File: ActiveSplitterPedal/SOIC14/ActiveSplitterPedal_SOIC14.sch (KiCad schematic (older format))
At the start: 9 parts, among them J1 MonoJack2Switch, J2 MonoJack2Switch, J3 MonoJack2Switch, J4 MonoJack2Switch, J5 MonoJack2Switch, J6 Barrel_Jack

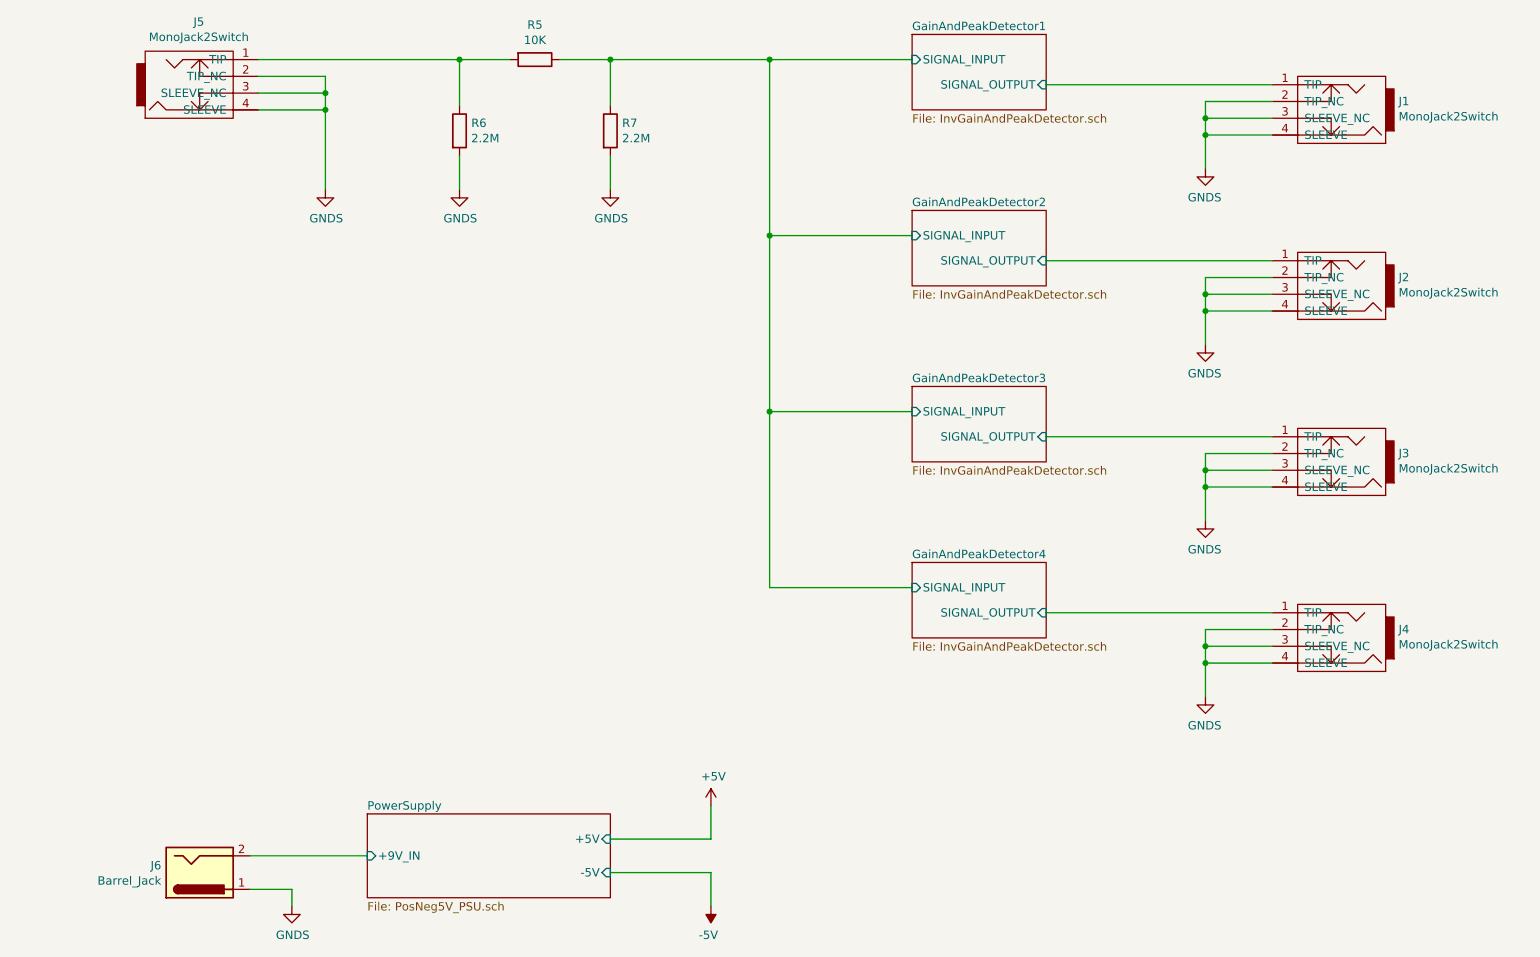
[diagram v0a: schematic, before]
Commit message: RevA HW updates
- Replaced SW Diode with Schottky Diode
- Added one charge pump IC per quad opamp (60mA each)
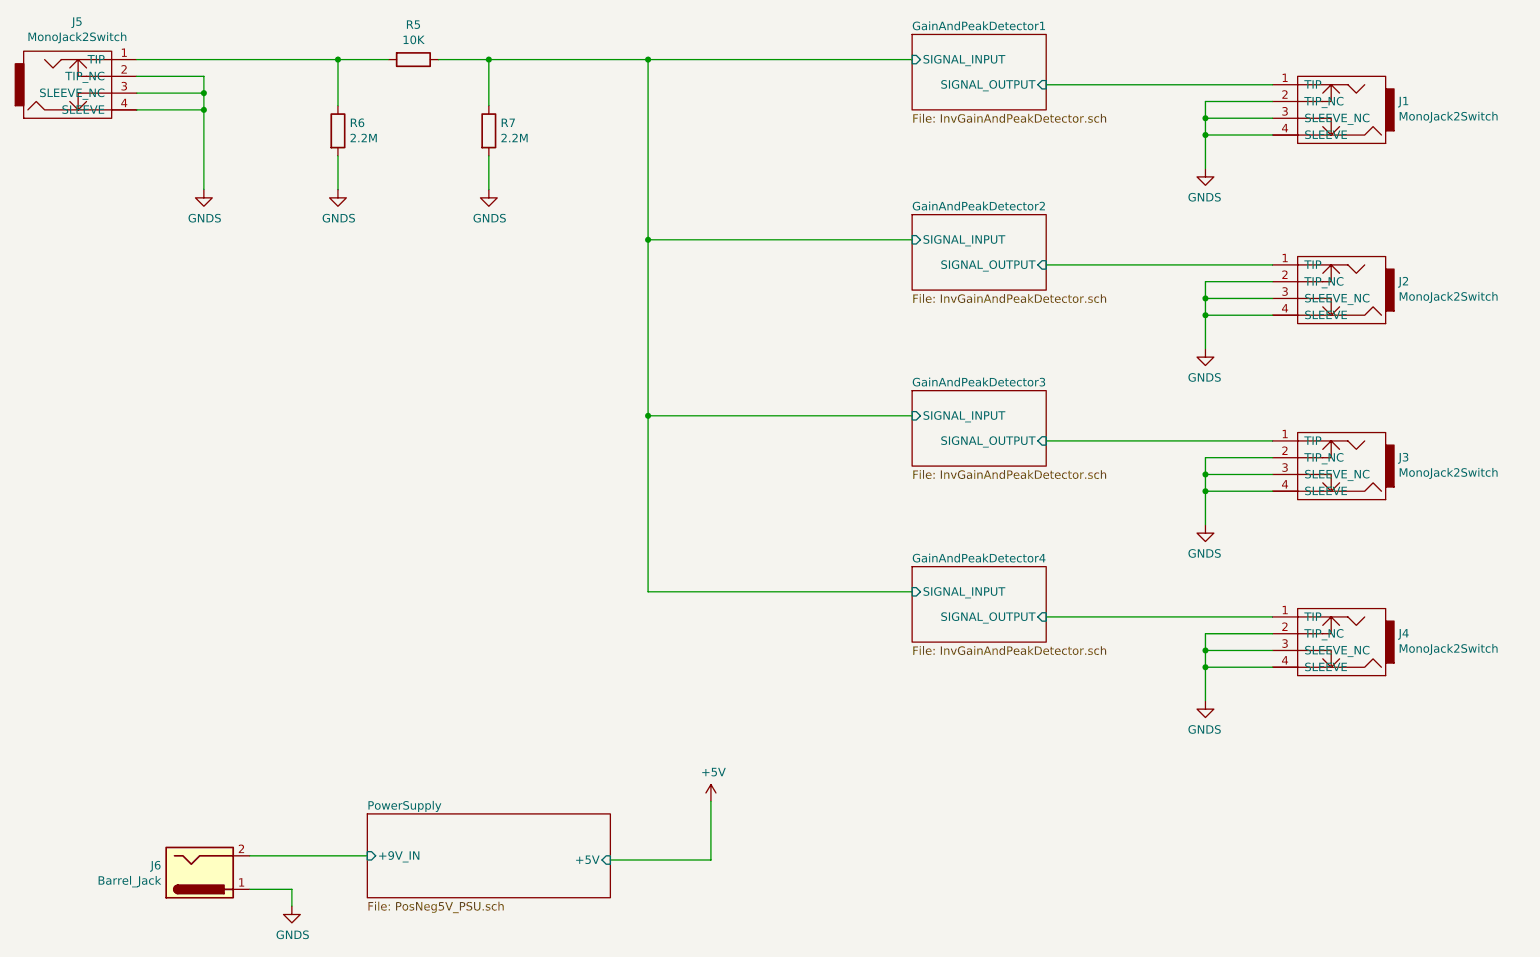
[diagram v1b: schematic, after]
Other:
- moved on the sheet: J2, J3, J4, J5, R5, R6, R7
